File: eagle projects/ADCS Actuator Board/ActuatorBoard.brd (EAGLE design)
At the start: 91 x 91 mm, 259 parts, among them J4 OSTVN08A150, J5 OSTVN08A150, J6 OSTVN08A150, U10 TVS991, U11 BD621F-E2, U12 ADS7841E_2K5, U13 ADS7841E_2K5, U15 TLV9051IDCKR, U16 BD621F-E2, U17 DRV10970_MOTOR_DRIVERDRV10970, U18 DRV10970_MOTOR_DRIVERDRV10970, U19 TLV9051IDCKR, U20 DRV10970_MOTOR_DRIVERDRV10970, U21 TLV9051IDCKR, U22 BD621F-E2, U23 TLV9051IDCKR, U24 TLV9051IDCKR, U25 ADS7841E_2K5, U26 TLV9051IDCKR, U27 ADS7841E_2K5, U28 TLV9051IDCKR, U29 TLV9051IDCKR, U30 TLV9051IDCKR, U31 TLV9051IDCKR, U32 TLV9051IDCKR, U4 ADS7841E_2K5, U6 TLV9051IDCKR, U7 TVS991, U8 TVS991, U9 ADS7841E_2K5

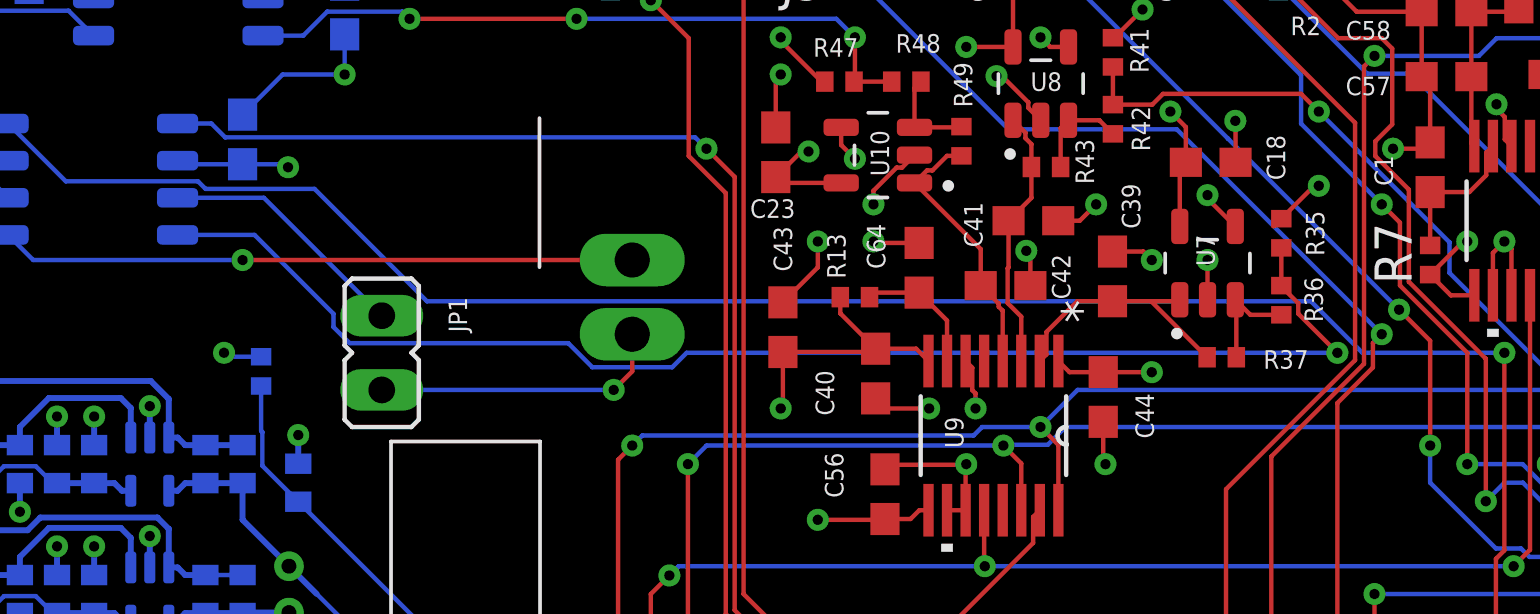
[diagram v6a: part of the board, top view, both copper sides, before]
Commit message: split the ground plane
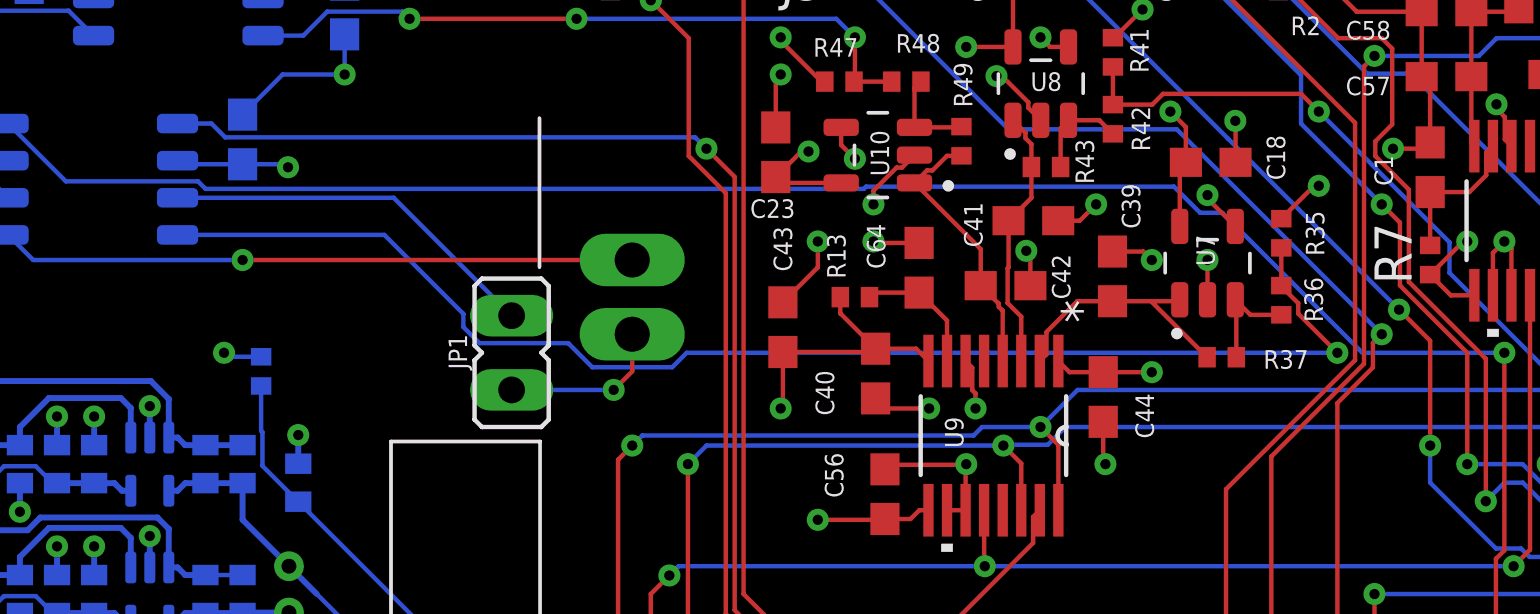
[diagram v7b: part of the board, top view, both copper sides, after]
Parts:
- moved JP1 4.44 mm to (28.9, 69.8)
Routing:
- net N$7: track 8.66 -> 13.1 mm
- net OUT2_X: track 10.1 -> 5.66 mm
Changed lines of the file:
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@@
 <layer number="13" name="Route13" color="21" fill="1" visible="no" active="no"/>
 <layer number="14" name="Route14" color="22" fill="1" visible="no" active="no"/>
-<layer number="15" name="POWER" color="48" fill="1" visible="yes" active="yes"/>
+<layer number="15" name="POWER" color="48" fill="1" visible="no" active="yes"/>
 <layer number="16" name="Bottom" color="1" fill="1" visible="yes" active="yes"/>
 <layer number="17" name="Pads" color="2" fill="1" visible="yes" active="yes"/>
@@
 <attribute name="SPICEPREFIX" value="C" x="23.1775" y="81.5975" size="1.778" layer="28" rot="MR90" display="off"/>
 </element>
-<element name="JP1" library="jumper" library_urn="urn:adsk.eagle:library:252" package="JP1" package3d_urn="urn:adsk.eagle:package:15455/1" value="" x="24.4475" y="69.85" smashed="yes">
-<attribute name="NAME" x="26.7335" y="71.755" size="0.635" layer="25" font="vector" ratio="10" rot="R270"/>
-<attribute name="POPULARITY" value="15" x="24.4475" y="69.85" size="1.778" layer="27" display="off"/>
-<attribute name="VALUE" x="27.3685" y="67.31" size="1.27" layer="27" ratio="10" rot="R90"/>
+<element name="JP1" library="jumper" library_urn="urn:adsk.eagle:library:252" package="JP1" package3d_urn="urn:adsk.eagle:package:15455/1" value="" x="28.8925" y="69.85" smashed="yes">
+<attribute name="NAME" x="26.7335" y="70.485" size="0.635" layer="25" font="vector" ratio="10" rot="R270"/>
+<attribute name="POPULARITY" value="15" x="28.8925" y="69.85" size="1.778" layer="27" display="off"/>
+<attribute name="VALUE" x="31.8135" y="67.31" size="1.27" layer="27" ratio="10" rot="R90"/>
 </element>
 <element name="JP2" library="jumper" library_urn="urn:adsk.eagle:library:252" package="JP1" package3d_urn="urn:adsk.eagle:package:15455/1" value="" x="76.835" y="65.405" smashed="yes" rot="R270">
@@
 <wire x1="58.00815" y1="69.85" x2="62.865" y2="69.85" width="0.1524" layer="16"/>
 <wire x1="18.15960625" y1="75.7186" x2="18.41840625" y2="75.4598" width="0.1524" layer="16"/>
-<wire x1="18.41840625" y1="75.4598" x2="22.14798125" y2="75.4598" width="0.1524" layer="16"/>
-<wire x1="22.14798125" y1="75.4598" x2="25.99418125" y2="71.6136" width="0.1524" layer="16"/>
-<wire x1="25.99418125" y1="71.6136" x2="56.24455" y2="71.6136" width="0.1524" layer="16"/>
-<wire x1="56.24455" y1="71.6136" x2="58.00815" y2="69.85" width="0.1524" layer="16"/>
 <wire x1="11.66" y1="77.695" x2="13.6364" y2="75.7186" width="0.1524" layer="16"/>
 <wire x1="13.6364" y1="75.7186" x2="18.15960625" y2="75.7186" width="0.1524" layer="16"/>
@@
 <wire x1="62.5757" y1="16.7993" x2="63.5" y2="15.875" width="0.1524" layer="1"/>
 <wire x1="63.5" y1="15.875" x2="63.5" y2="11.43" width="0.1524" layer="1"/>
+<wire x1="40.94665" y1="75.4598" x2="41.02365" y2="75.5368" width="0.1524" layer="16"/>
+<wire x1="52.45365" y1="74.6407" x2="53.21745" y2="74.6407" width="0.1524" layer="16"/>
+<wire x1="41.02365" y1="75.5368" x2="51.55755" y2="75.5368" width="0.1524" layer="16"/>
+<wire x1="51.55755" y1="75.5368" x2="52.45365" y2="74.6407" width="0.1524" layer="16"/>
+<wire x1="18.41840625" y1="75.4598" x2="40.94665" y2="75.4598" width="0.1524" layer="16"/>
+<wire x1="53.21745" y1="74.6407" x2="58.00815" y2="69.85" width="0.1524" layer="16"/>
 </signal>
 <signal name="MAG_X_RIN">
@@
 <wire x1="27.5816" y1="32.6743" x2="26.035" y2="32.6743" width="0.1524" layer="16"/>
 <via x="26.035" y="32.6743" extent="1-16" drill="0.35"/>
+<polygon width="0.1524" layer="2" pour="cutout">
+<vertex x="31.115" y="20.955"/>
+<vertex x="29.21" y="20.955"/>
+<vertex x="29.21" y="18.415"/>
+<vertex x="24.765" y="13.97"/>
+<vertex x="24.765" y="0"/>
+<vertex x="26.67" y="0"/>
+<vertex x="26.67" y="12.7"/>
+<vertex x="31.115" y="17.145"/>
+</polygon>
+<polygon width="0.1524" layer="2" pour="cutout">
+<vertex x="34.29" y="51.435"/>
+<vertex x="32.385" y="51.435"/>
+<vertex x="32.385" y="59.69"/>
+<vertex x="23.495" y="68.58"/>
+<vertex x="22.86" y="69.215"/>
+<vertex x="3.81" y="69.215"/>
+<vertex x="3.81" y="71.12"/>
+<vertex x="24.13" y="71.12"/>
+<vertex x="34.29" y="60.96"/>
+</polygon>
 </signal>
 <signal name="+5V">
@@
 <contactref element="U16" pad="8"/>
 <wire x1="55.2325" y1="73.44" x2="55.2325" y2="72.15" width="0.1524" layer="1"/>
-<wire x1="17.46" y1="73.885" x2="20.095" y2="73.885" width="0.1524" layer="16"/>
-<wire x1="22.7965" y1="70.73071875" x2="23.34701875" y2="70.1802" width="0.1524" layer="16"/>
-<wire x1="22.7965" y1="71.1835" x2="22.7965" y2="70.73071875" width="0.1524" layer="16"/>
 <wire x1="55.245" y1="72.15" x2="55.2325" y2="72.15" width="0.1524" layer="1"/>
-<wire x1="20.095" y1="73.885" x2="22.7965" y2="71.1835" width="0.1524" layer="16"/>
 <via x="57.15" y="69.85" extent="1-16" drill="0.35"/>
 <wire x1="31.6525125" y1="69.3564" x2="34.3874875" y2="69.3564" width="0.1524" layer="16"/>
@@
 <wire x1="55.245" y1="72.1107875" x2="55.245" y2="72.15" width="0.1524" layer="1"/>
 <wire x1="55.8111" y1="71.5446875" x2="55.245" y2="72.1107875" width="0.1524" layer="1"/>
-<wire x1="23.34701875" y1="70.1802" x2="30.8287125" y2="70.1802" width="0.1524" layer="16"/>
+<wire x1="27.2415" y1="71.1835" x2="27.2415" y2="70.73071875" width="0.1524" layer="16"/>
+<wire x1="27.2415" y1="70.73071875" x2="27.79201875" y2="70.1802" width="0.1524" layer="16"/>
+<wire x1="27.79201875" y1="70.1802" x2="30.8287125" y2="70.1802" width="0.1524" layer="16"/>
+<wire x1="17.46" y1="73.885" x2="24.54" y2="73.885" width="0.1524" layer="16"/>
+<wire x1="24.54" y1="73.885" x2="27.2415" y2="71.1835" width="0.1524" layer="16"/>
 </signal>
 <signal name="MAG_CUR_SEN_Y">
@@
 <contactref element="JP1" pad="1"/>
 <contactref element="JX" pad="2"/>
-<wire x1="24.4475" y1="68.58" x2="32.385" y2="68.58" width="0.1524" layer="16"/>
+<wire x1="28.8925" y1="68.58" x2="32.385" y2="68.58" width="0.1524" layer="16"/>
 <via x="32.385" y="68.58" extent="1-16" drill="0.35"/>
 <wire x1="32.385" y1="68.58" x2="33.02" y2="69.215" width="0.1524" layer="1"/>
@@
 <contactref element="JP1" pad="2"/>
 <contactref element="U16" pad="7"/>
-<wire x1="17.46" y1="75.155" x2="20.4125" y2="75.155" width="0.1524" layer="16"/>
-<wire x1="20.4125" y1="75.155" x2="24.4475" y2="71.12" width="0.1524" layer="16"/>
+<wire x1="17.46" y1="75.155" x2="24.8575" y2="75.155" width="0.1524" layer="16"/>
+<wire x1="24.8575" y1="75.155" x2="28.8925" y2="71.12" width="0.1524" layer="16"/>
 </signal>
 <signal name="N$8">
